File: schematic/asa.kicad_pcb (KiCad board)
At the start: 2 copper layers, 22 parts, among them K1 CONN_3, K2 CONN_3, Q1 KT815, Q2 KT814

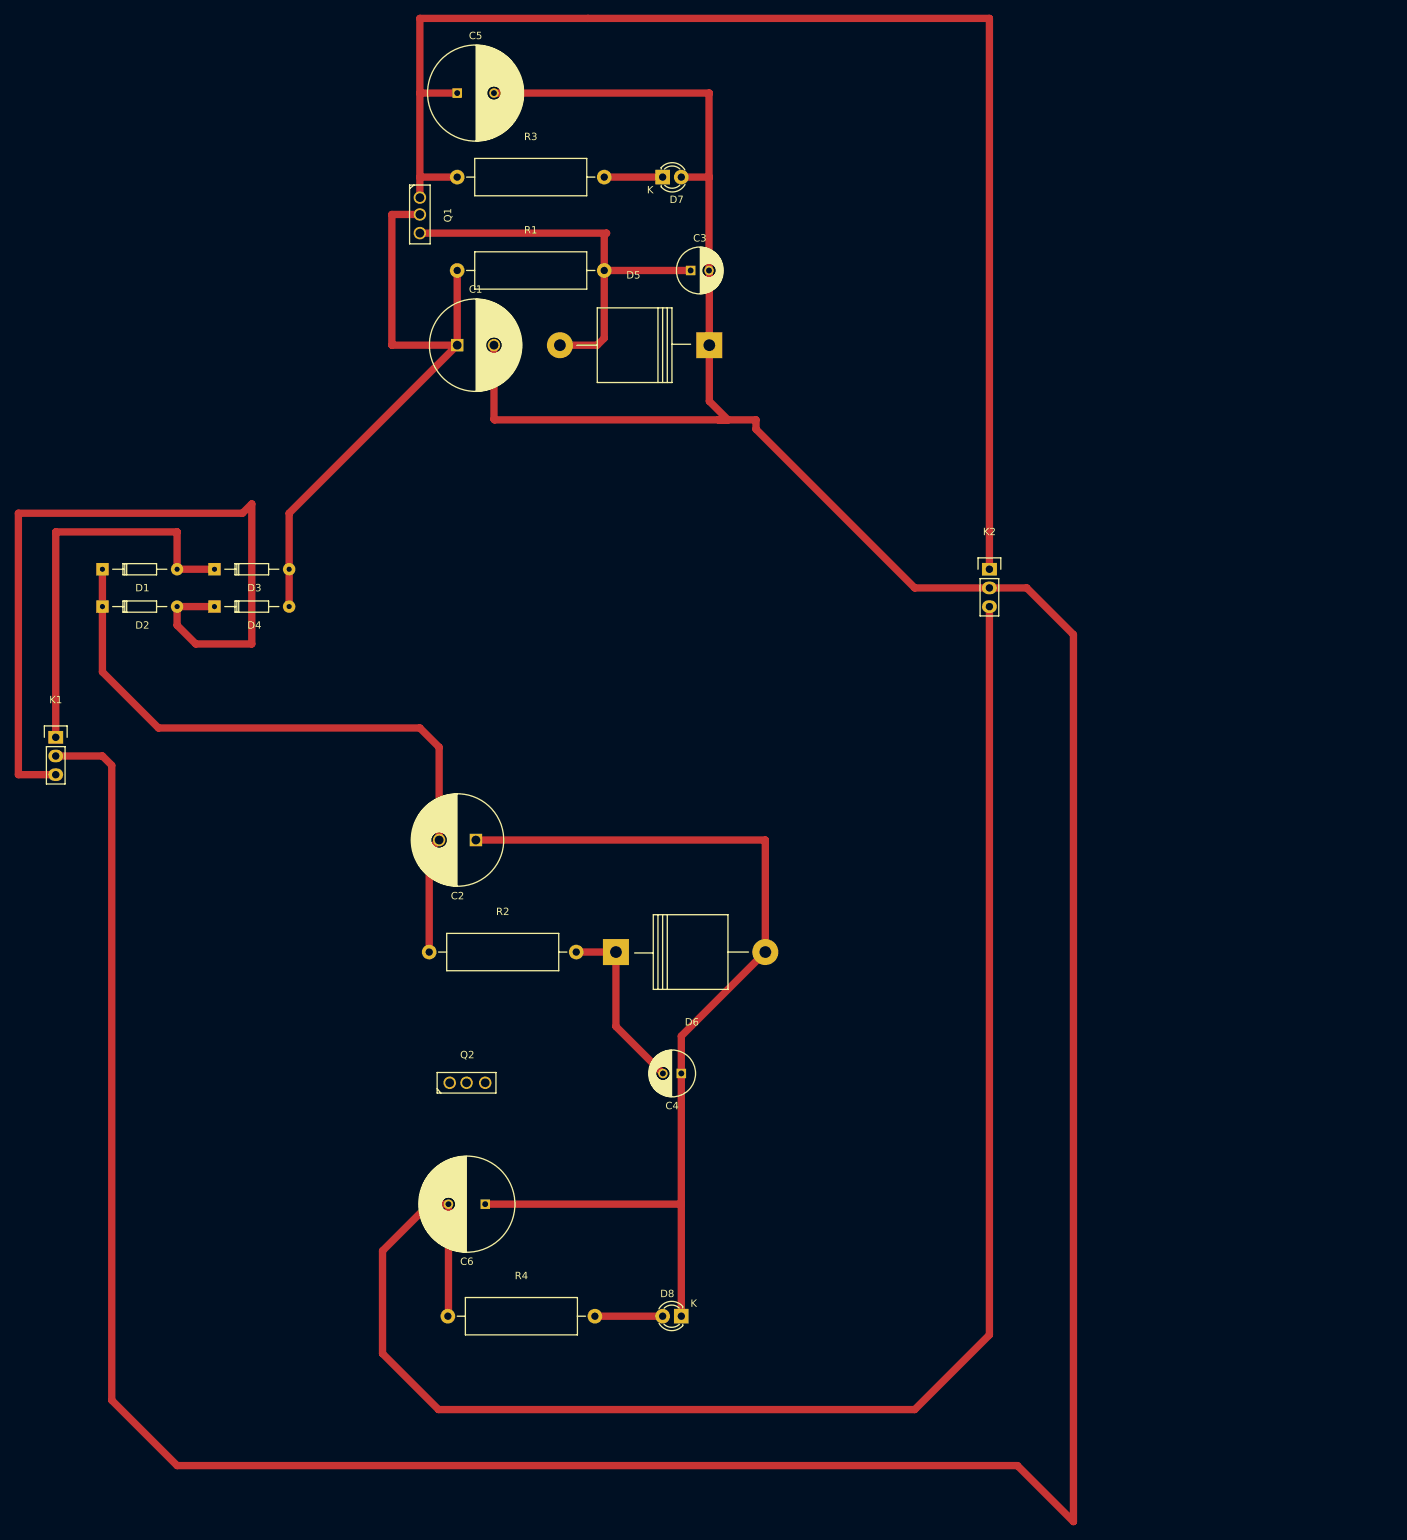
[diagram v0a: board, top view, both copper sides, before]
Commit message: Trace route the schematic on PCB 170x52mm.
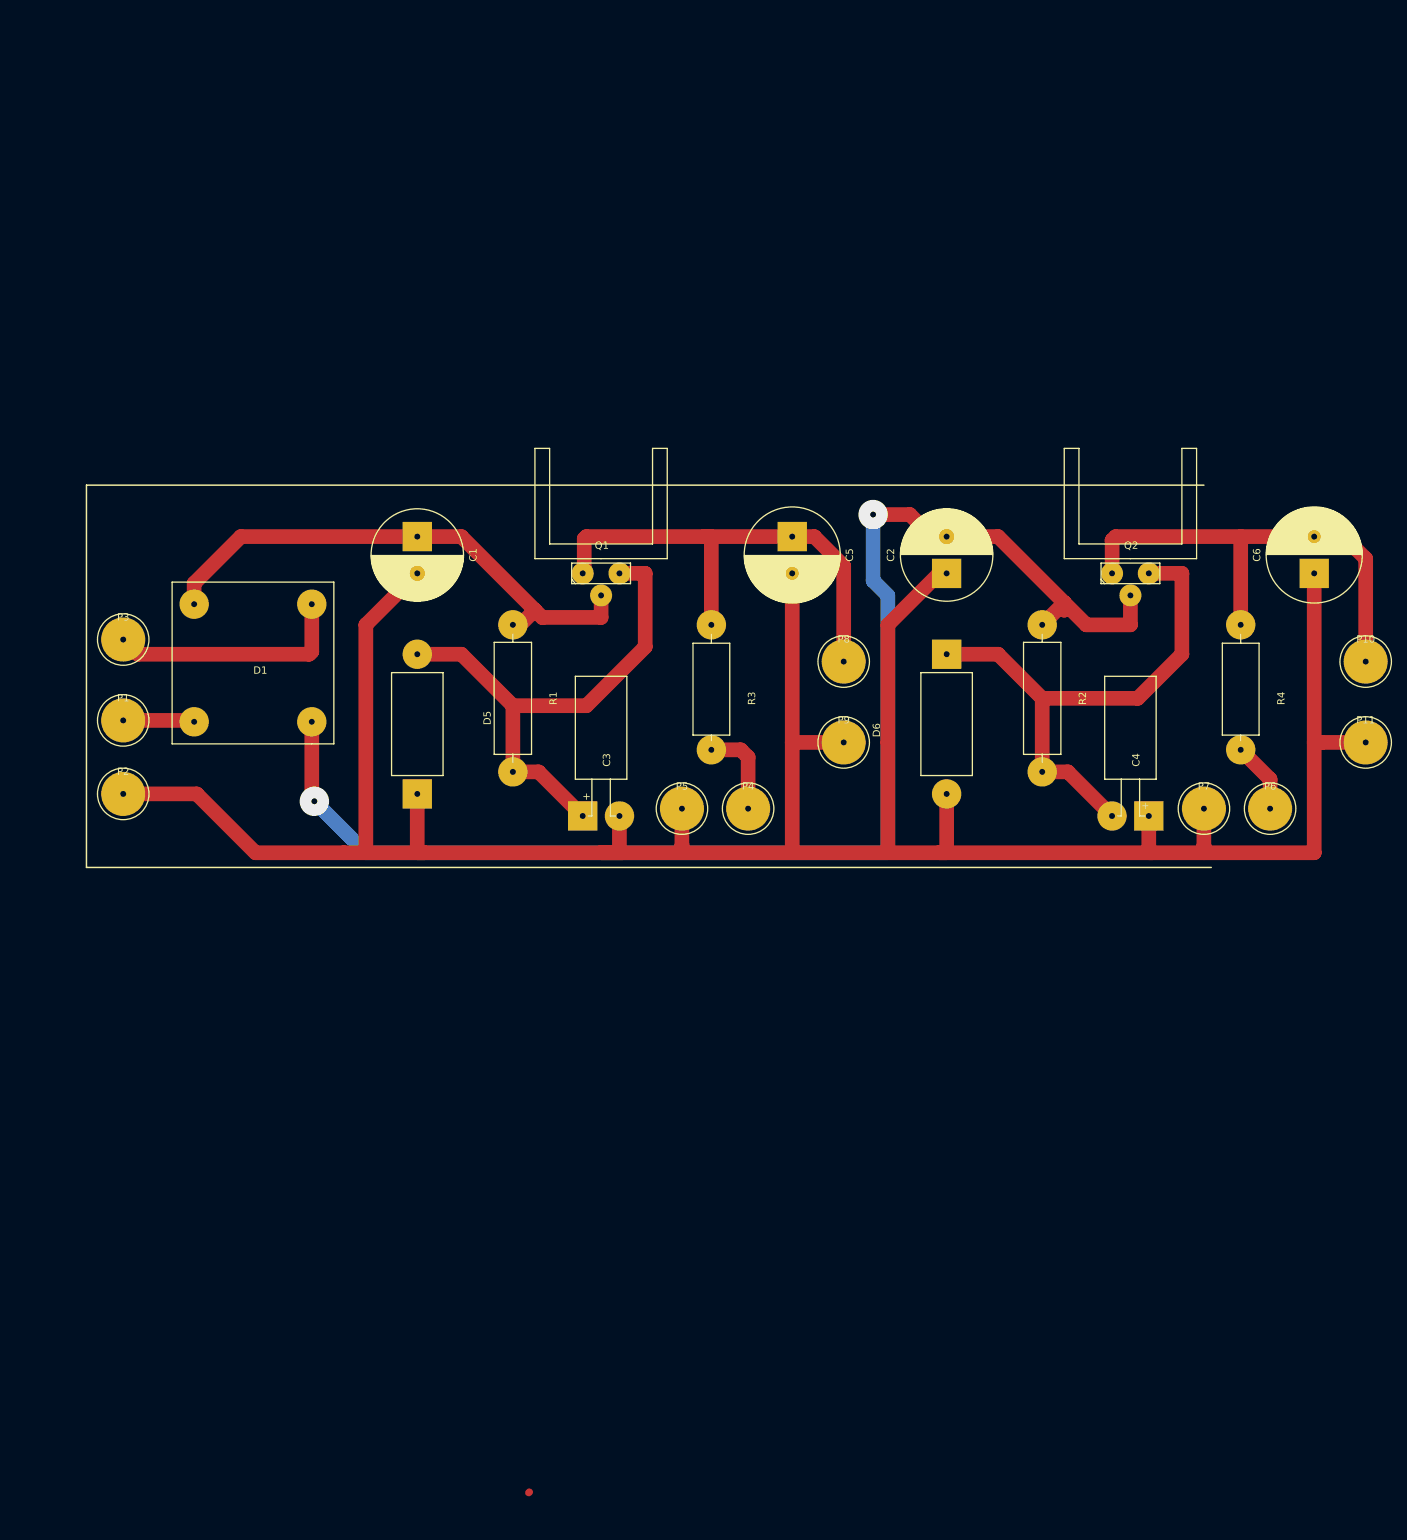
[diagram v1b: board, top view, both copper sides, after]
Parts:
- removed D2, D3, D4: DIODE, Diodes_ThroughHole:Diode_DO-35_SOD27_Horizontal_RM10
- removed D7, D8: LED, LEDs:LED-3MM
- removed K1, K2: CONN_3, Pin_Headers:Pin_Header_Straight_1x03
- added P1: CONN_01X01, footprints:1pin_big, F.Cu at (93.0, 112.0)
- added P10: CONN_01X01, footprints:1pin_big, F.Cu at (262.0, 104.0)
- added P11: CONN_01X01, footprints:1pin_big, F.Cu at (262.0, 115.0)
- added P2: CONN_01X01, footprints:1pin_big, F.Cu at (93.0, 122.0)
- added P3: CONN_01X01, footprints:1pin_big, F.Cu at (93.0, 101.0)
- added P4: CONN_01X01, footprints:1pin_big, F.Cu at (178.0, 124.0)
- added P5: CONN_01X01, footprints:1pin_big, F.Cu at (169.0, 124.0)
- added P6: CONN_01X01, footprints:1pin_big, F.Cu at (249.0, 124.0)
- added P7: CONN_01X01, footprints:1pin_big, F.Cu at (240.0, 124.0)
- added P8: CONN_01X01, footprints:1pin_big, F.Cu at (191.0, 104.0)
- added P9: CONN_01X01, footprints:1pin_big, F.Cu at (191.0, 115.0)
- C1, C2: footprint Capacitors_ThroughHole:C_Radial_D12.5_L25_P5 -> footprints:C_Radial_D12.5_L25_P5_1000u
- C3: footprint Capacitors_ThroughHole:C_Radial_D6.3_L11.2_P2.5 -> footprints:C100u_horiz_mirror
- C4: footprint Capacitors_ThroughHole:C_Radial_D6.3_L11.2_P2.5 -> footprints:C100u_horiz
- C5, C6: footprint Capacitors_ThroughHole:C_Radial_D13_L21_P5 -> footprints:C_Radial_D13_L21_P5_470u
- D1: value DIODE -> Diode_Bridge; footprint Diodes_ThroughHole:Diode_DO-35_SOD27_Horizontal_RM10 -> footprints:Diode_Bridge_22x22
- D5, D6: footprint Diodes_ThroughHole:Diode_P600_Horizontal -> footprints:Diode_P600_Horizontal_D814
- Q1, Q2: footprint TO_SOT_Packages_THT:SOT126_SOT32_Housing_Vertical -> footprints:SOT126_SOT32_Housing_Vertical_KT81x
- R1, R2: footprint Resistors_ThroughHole:Resistor_Horizontal_RM20mm -> footprints:Resistor_Horizontal_RM20mm_0.5W
- R3, R4: value R -> 1200 0.125W; footprint Resistors_ThroughHole:Resistor_Horizontal_RM20mm -> footprints:Resistor_Horizontal_RM20mm_0.25W
- moved R4 143.1 mm to (245.0, 99.0), turned to 270 degrees
- moved C6 141.7 mm to (255.0, 92.0), turned to 90 degrees
- moved Q2 113.8 mm to (230.0, 92.0)
- moved R2 94.5 mm to (218.0, 99.0), turned to 270 degrees
- moved C5 75.6 mm to (184.0, 87.0), turned to 270 degrees
- moved C3 75.2 mm to (158.0, 125.0), turned to 180 degrees
- moved C2 73.6 mm to (205.0, 92.0), turned to 90 degrees
- moved D5 72.8 mm to (133.0, 122.0), turned to 90 degrees
- moved C4 70.4 mm to (230.0, 125.0)
- moved R3 70.0 mm to (173.0, 99.0), turned to 270 degrees
- moved D6 60.5 mm to (205.0, 103.0), turned to 270 degrees
- moved Q1 54.7 mm to (158.0, 92.0), turned to 0 degrees
- moved R1 48.8 mm to (146.0, 99.0), turned to 270 degrees
- moved D1 35.2 mm to (118.7, 112.2), turned to 180 degrees
- moved C1 26.6 mm to (133.0, 87.0), turned to 270 degrees
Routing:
- net Net-(C1-Pad2): track 670.2 -> 387.8 mm
- net Net-(C6-Pad2): track 229.8 -> 66.4 mm
- net Net-(C5-Pad1): track 186.9 -> 67.8 mm
- net Net-(D2-Pad2): track 110.8 -> 0.00 mm
- net Net-(C2-Pad2): track 92.4 -> 190.1 mm, vias 0 -> 2
- net Net-(C4-Pad2): track 24.6 -> 74.5 mm
- net Net-(D1-Pad2): track 54.6 -> 33.1 mm
- net Net-(C3-Pad1): track 58.0 -> 71.7 mm
- net Net-(C1-Pad1): track 85.7 -> 72.2 mm
- net Net-(D1-Pad4): track 0.00 -> 9.73 mm
- net Net-(P4-Pad1): track 7.94 -> 12.4 mm
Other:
- net class Default: trace_width 1 -> 2; via_dia 0.6 -> 4; via_drill 0.4 -> 0.8

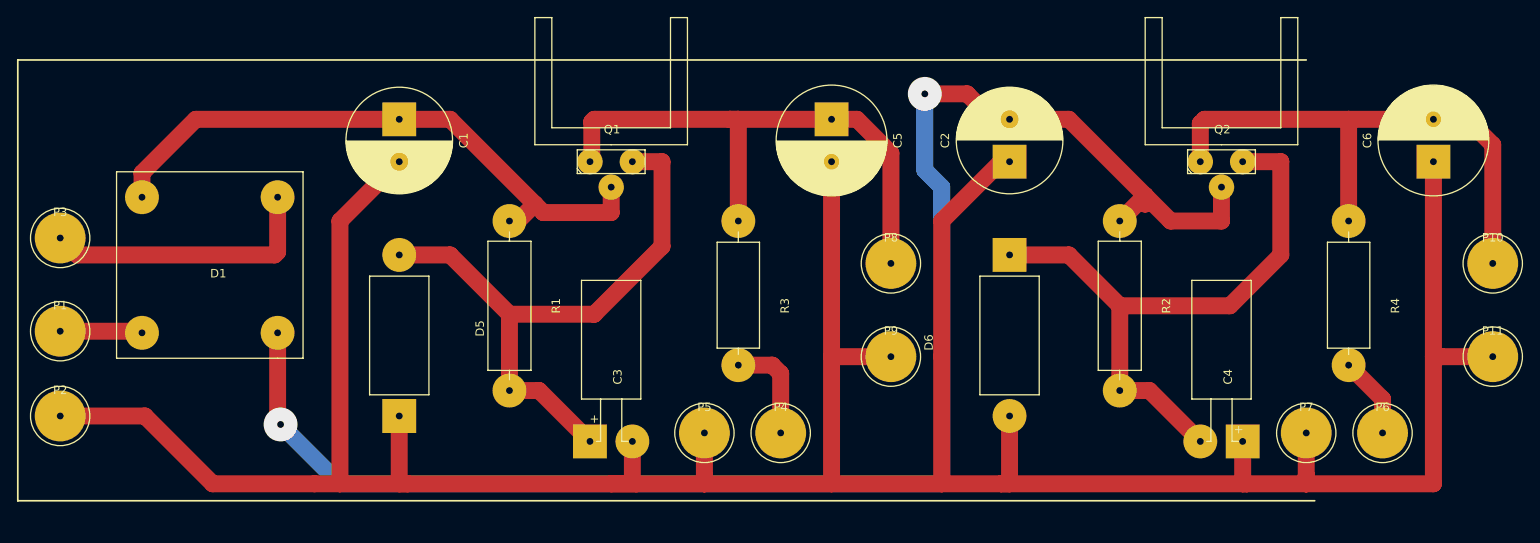
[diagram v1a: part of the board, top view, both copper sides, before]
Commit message: Reduce PCB size to 140x52mm.
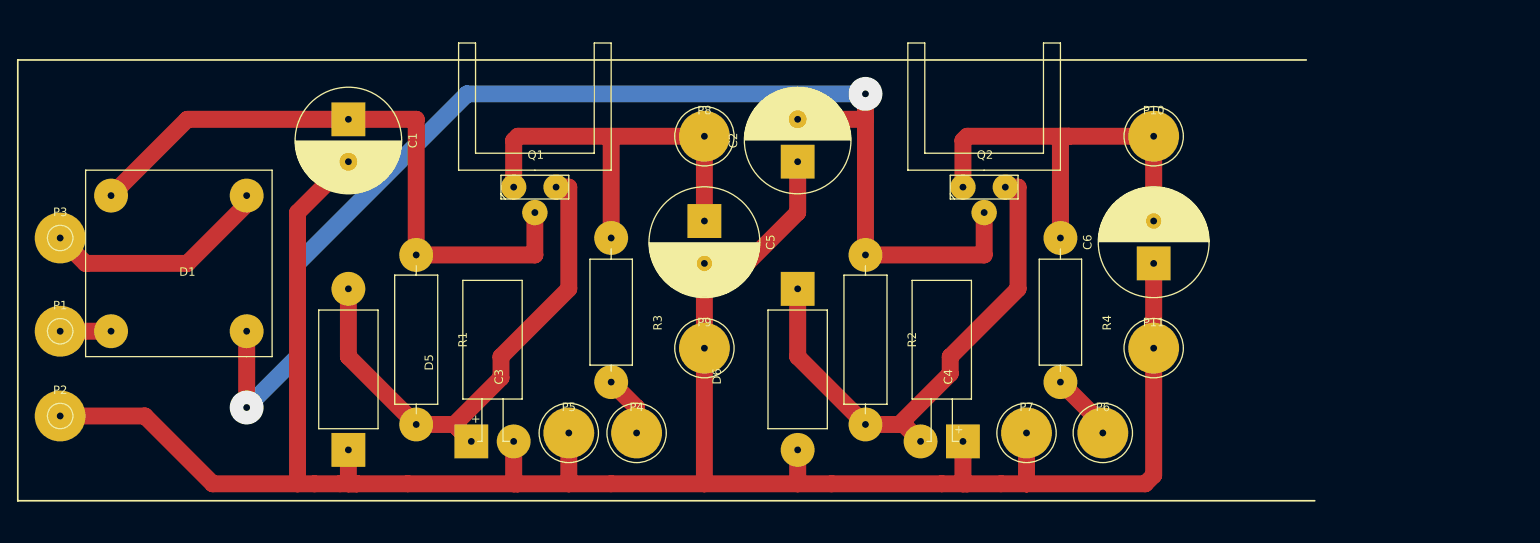
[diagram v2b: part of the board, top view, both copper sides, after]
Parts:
- moved P10 42.7 mm to (222.0, 89.0)
- moved P11 40.0 mm to (222.0, 114.0)
- moved C6 35.1 mm to (222.0, 104.0)
- moved R4 34.1 mm to (211.0, 101.0)
- moved C4 33.0 mm to (197.0, 125.0)
- moved P6 33.0 mm to (216.0, 124.0)
- moved P7 33.0 mm to (207.0, 124.0)
- moved R2 30.3 mm to (188.0, 103.0)
- moved Q2 28.2 mm to (202.0, 95.0)
- moved P8 26.6 mm to (169.0, 89.0)
- moved D6 25.3 mm to (180.0, 107.0)
- moved C2 25.0 mm to (180.0, 92.0)
- moved P9 22.0 mm to (169.0, 114.0)
- moved C5 19.2 mm to (169.0, 99.0)
- moved P4 17.0 mm to (161.0, 124.0)
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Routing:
- net Net-(C1-Pad2): track 387.8 -> 277.7 mm
- net Net-(C2-Pad2): track 190.1 -> 149.8 mm
- net Net-(C5-Pad1): track 67.8 -> 50.2 mm
- net Net-(C6-Pad2): track 66.4 -> 51.2 mm
- net Net-(C4-Pad2): track 74.5 -> 61.9 mm
- net Net-(C3-Pad1): track 71.7 -> 64.6 mm
- net Net-(D1-Pad2): track 33.1 -> 27.1 mm
- net Net-(P4-Pad1): track 12.4 -> 7.24 mm
- net Net-(D1-Pad4): track 9.73 -> 6.00 mm
- net Net-(C1-Pad1): track 72.2 -> 74.7 mm
- net Net-(P6-Pad1): track 9.66 -> 8.07 mm
